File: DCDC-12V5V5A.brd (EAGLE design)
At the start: 40 x 23 mm, 37 parts, among them CN2 2828XX-2282834-2, CN3 2828XX-2282834-2, Q10 NMOSFET, Q9 NMOSFET, U1 LM3150MHX/NOPB

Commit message: Renamed 12V line to Vin. Generated CAM files.
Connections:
- net 12V renamed VIN
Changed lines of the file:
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@@
 </elements>
 <signals>
-<signal name="12V" airwireshidden="yes">
+<signal name="VIN" airwireshidden="yes">
 <contactref element="Q9" pad="4"/>
 <contactref element="U1" pad="2"/>

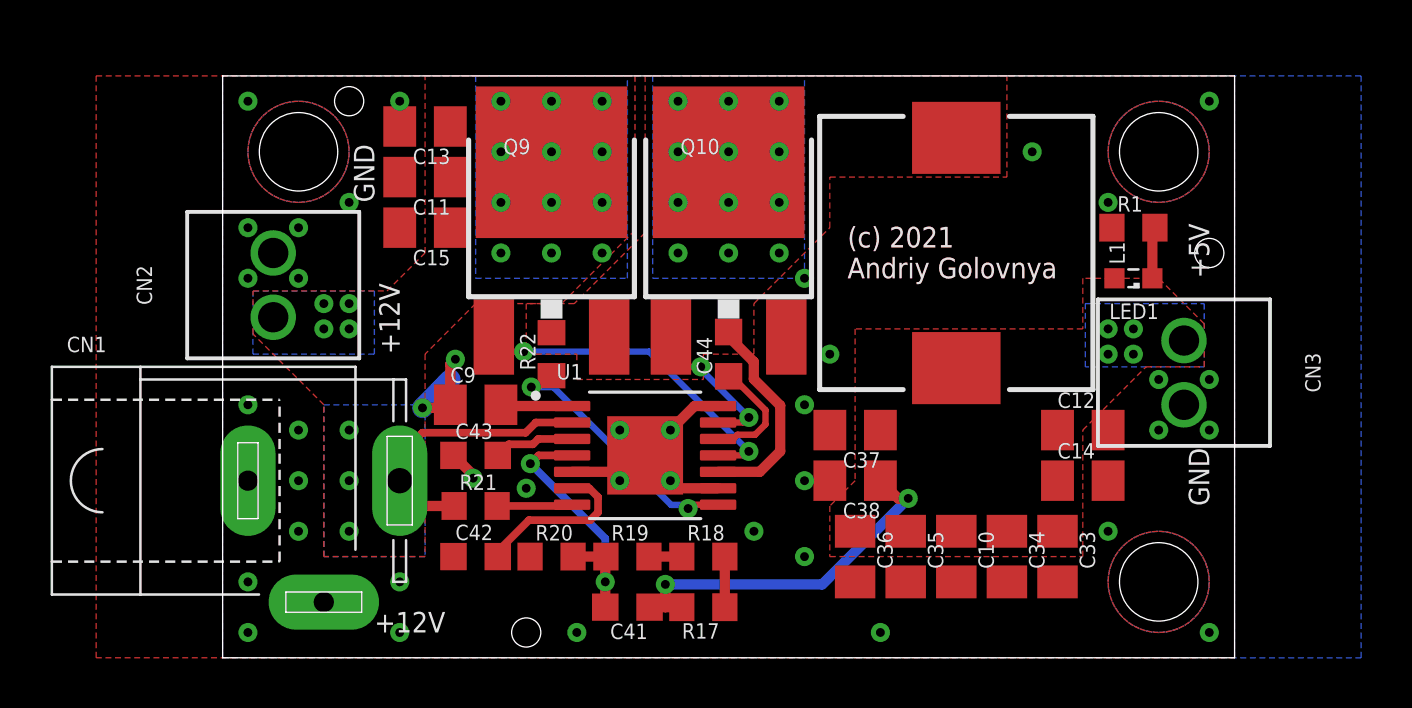
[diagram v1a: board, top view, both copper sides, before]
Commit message: Made new layout of DC-DC board. Improved XLS calculator. Generated CAM files. Generated BoM and PnP files. Generated PNG preview. Generated PDF schematics.
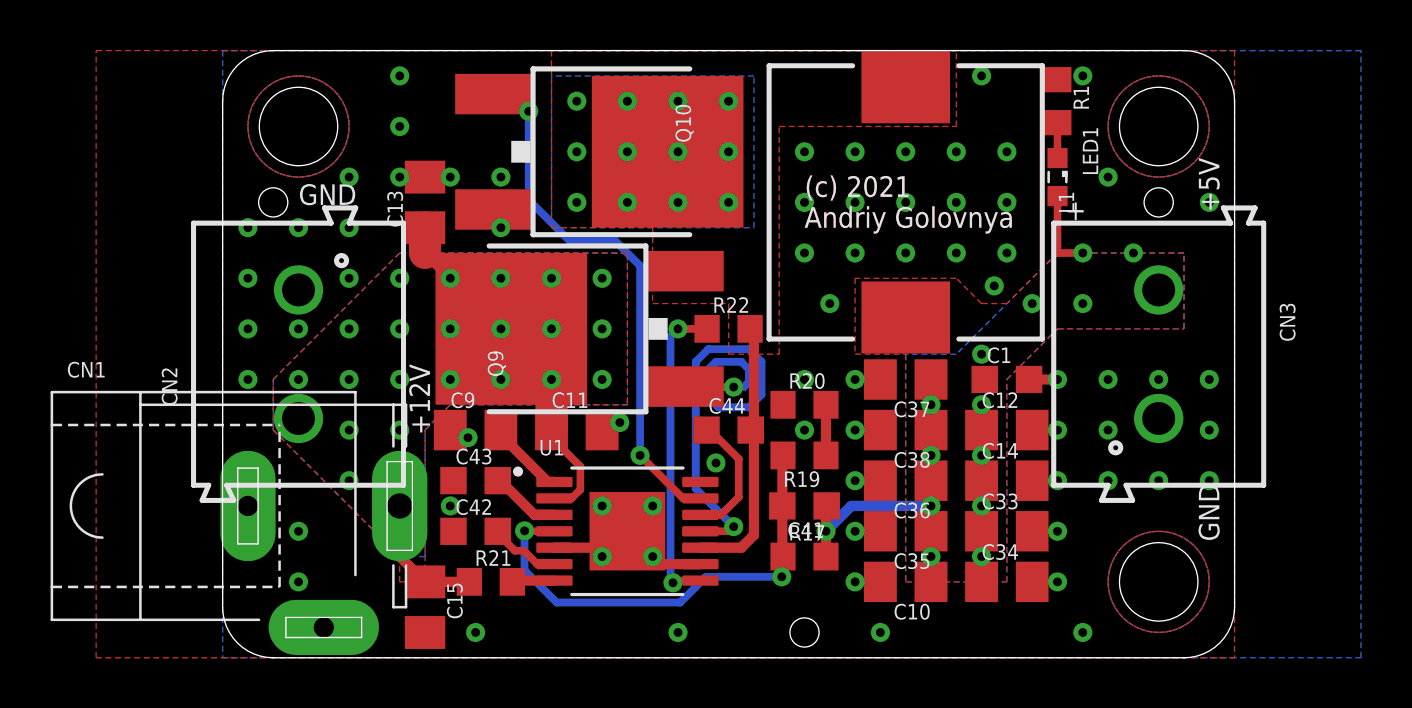
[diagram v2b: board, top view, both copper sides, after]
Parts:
- removed R18: 3k, rcl:R0603
- added C1: 1nF, rcl:C0603K
- CN2, CN3: value 2828XX-2282834-2 -> (none); device Connector:TERMBLK_254-2N -> Wurth_Connectors_WR-TBL Rising Cage Clamp:691213510002
- R1: value 3k -> 2k
- R17: value 68k -> 75k
- R19: value 3k -> 100
- moved C15 15.0 mm to (8.00, 2.00), turned to 270 degrees
- moved C11 11.7 mm to (14.0, 9.00), turned to 0 degrees
- moved R20 11.7 mm to (23.0, 10.0)
- moved HOLE3 11.0 mm to (23.0, 1.00)
- moved C41 8.06 mm to (23.0, 6.00)
- moved R19 8.06 mm to (23.0, 8.00), turned to 180 degrees
- moved R22 7.07 mm to (20.0, 13.0), turned to 0 degrees
- moved R1 5.83 mm to (33.0, 22.0), turned to 270 degrees
- moved HOLE2 5.00 mm to (2.00, 18.0)
- moved LED1 5.00 mm to (33.0, 19.0), turned to 270 degrees
- moved Q9 5.00 mm to (13.0, 13.0), turned to 90 degrees
- moved Q10 4.47 mm to (16.0, 20.0), turned to 270 degrees
- moved R17 4.47 mm to (23.0, 4.00), turned to 0 degrees
- moved CN2 4.12 mm to (3.00, 12.0)
- moved C36 3.61 mm to (27.0, 7.00), turned to 180 degrees
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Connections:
- net N$16 renamed BUCK_SS
- net N$18 renamed BUCK_EN
- net N$19 renamed BUCK_VCC
- net N$21 renamed BUCK_RON
- net N$23 renamed BUCK_BST
- net N$8 renamed BUCK_ILIM
- removed net N$13: R18.1, R19.2
- removed net N$9: R17.1, R18.2
- new net N$2: R19.1, R20.2
- net 5V: now also C1.1
- net BUCK_FB: now also R17.1, R19.2; no longer R19.1, R20.2
- net GND: now also C1.2
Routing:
- net BUCK_LG: track 6.23 -> 21.3 mm
- net BUCK_HG: track 13.3 -> 21.3 mm
- net BUCK_FB: track 11.0 -> 18.7 mm
- net GND: track 12.1 -> 5.16 mm, vias 40 -> 70
- net 5V: track 14.6 -> 9.82 mm, vias 6 -> 14
- net BUCK_SS: track 6.58 -> 2.83 mm
- net VIN: track 10.9 -> 13.6 mm, vias 19 -> 21
- net BUCK_SW: track 8.35 -> 10.6 mm
- net BUCK_ILIM: track 10.4 -> 12.5 mm
- net N$9: track 2.00 -> 0.00 mm
- net N$2: track 0.00 -> 2.00 mm
- net N$13: track 1.30 -> 0.00 mm
- net BUCK_RON: track 2.99 -> 1.72 mm
- net N$1: track 2.04 -> 1.40 mm
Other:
- board size 40 x 23 mm -> 40 x 24 mm
- board text added: "+"
- board text added: "DCDC-12V5V5A-0011"
- board text removed: "DCDC-12V5V5A-0010"

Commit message: Improved layout of DC-DC board. Rotated input terminal. Improved XLS calculator. Generated CAM files. Generated BoM and PnP files. Generated PNG preview. Generated PDF schematics.
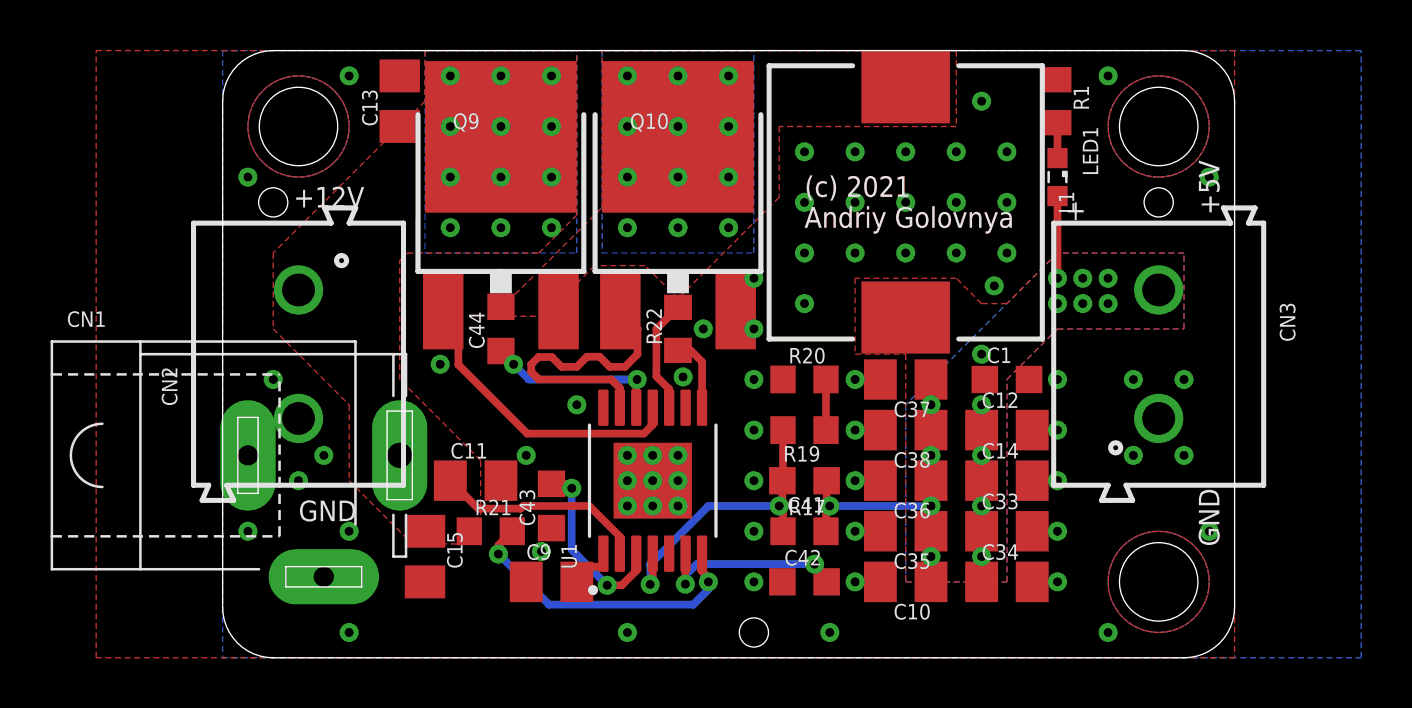
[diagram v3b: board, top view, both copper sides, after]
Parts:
- moved C42 13.2 mm to (23.0, 3.00)
- moved C44 9.85 mm to (11.0, 13.0), turned to 90 degrees
- moved C9 6.71 mm to (13.0, 3.00)
- moved Q9 6.32 mm to (11.0, 19.0), turned to 0 degrees
- moved C11 4.47 mm to (10.0, 7.00)
- moved C13 4.12 mm to (7.00, 22.0)
- moved C43 3.16 mm to (13.0, 6.00), turned to 90 degrees
- moved Q10 2.24 mm to (18.0, 19.0), turned to 0 degrees
- moved U1 2.24 mm to (17.0, 7.00), turned to 90 degrees
- moved C15 2.00 mm to (8.00, 4.00)
- moved CN1 2.00 mm to (4.00, 8.00)
- moved HOLE3 2.00 mm to (21.0, 1.00)
- moved R21 2.00 mm to (10.6, 5.00)
- moved R22 2.00 mm to (18.0, 13.0), turned to 90 degrees
- moved C41 1.00 mm to (23.0, 7.00)
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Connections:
- net GND: now also CN2.2; no longer CN2.1
- net VIN: now also CN2.1; no longer CN2.2
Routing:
- net BUCK_RON: track 1.72 -> 12.0 mm, vias 0 -> 2
- net BUCK_ILIM: track 12.5 -> 2.95 mm, vias 2 -> 0
- net BUCK_LG: track 21.3 -> 11.8 mm, vias 2 -> 0
- net BUCK_HG: track 21.3 -> 12.0 mm, vias 2 -> 0
- net BUCK_FB: track 18.7 -> 12.2 mm
- net BUCK_SW: track 10.6 -> 4.53 mm
- net VIN: track 13.6 -> 8.38 mm, vias 21 -> 12
- net GND: track 5.16 -> 0.00 mm, vias 70 -> 69
- net BUCK_SS: track 2.83 -> 7.75 mm, vias 0 -> 2
- net BUCK_EN: track 2.80 -> 7.35 mm, vias 0 -> 2
- net BUCK_BST: track 5.06 -> 6.99 mm, vias 0 -> 2
- net BUCK_VCC: track 3.08 -> 1.73 mm
- net 5V: track 9.82 -> 9.36 mm, vias 14 -> 16

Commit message: Moved some texts and tooling holes a bit. Generated CAM files. Generated PNG preview. Generated PDF schematics. Renamed BoM and PnP files.
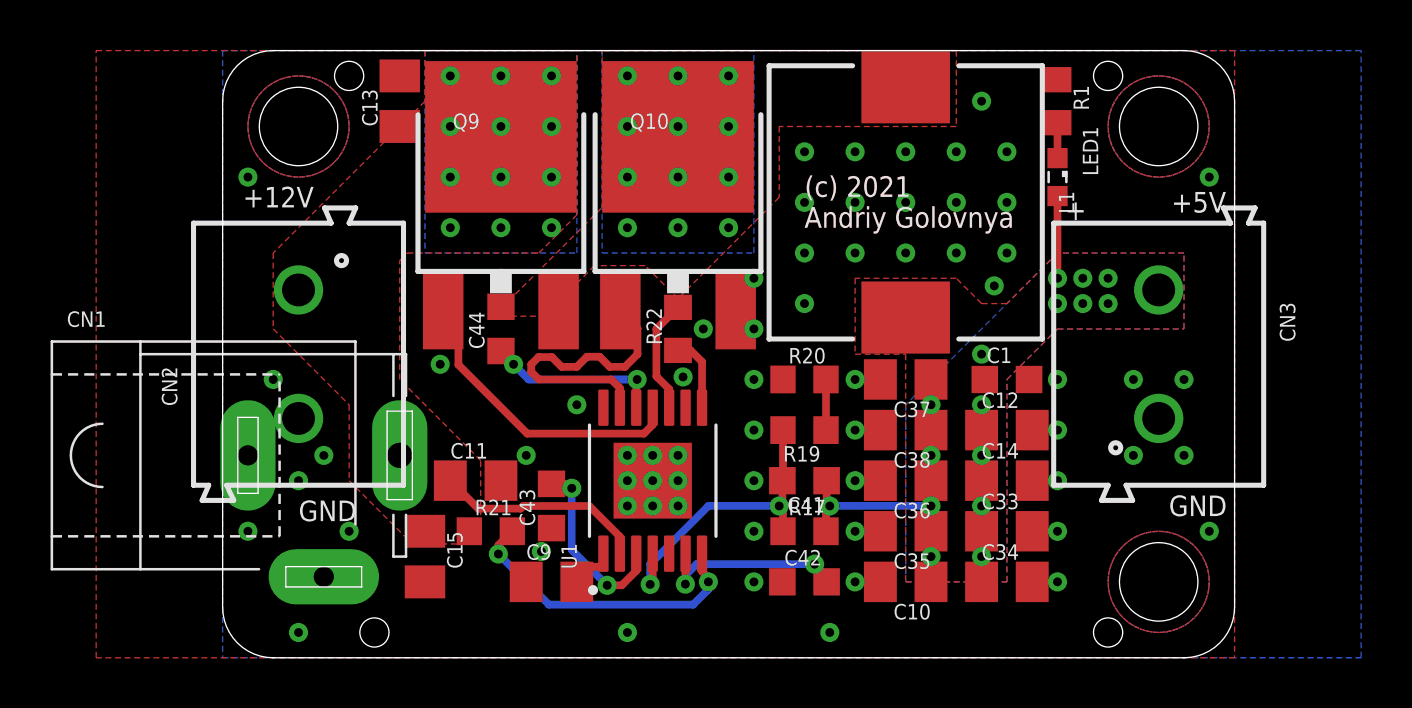
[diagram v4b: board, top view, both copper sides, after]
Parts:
- added HOLE4: TOOLINGHOLE, _my_fiducia:TOOLING-HOLE
- moved HOLE3 15.0 mm to (6.00, 1.00)
- moved HOLE2 5.83 mm to (5.00, 23.0)
- moved HOLE1 5.39 mm to (35.0, 23.0)
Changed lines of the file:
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@@
 <drawing>
 <settings>
-<setting alwaysvectorfont="yes"/>
+<setting alwaysvectorfont="no"/>
 <setting verticaltext="up"/>
 </settings>
@@
 <hole x="37" y="3" drill="3.1"/>
 <text x="33" y="20" size="1.6764" layer="22" font="vector" ratio="20" rot="MR0">DCDC-12V5V5A-0011</text>
-<text x="2.8" y="17.8" size="0.8128" layer="21" font="vector">+12V</text>
+<text x="0.8" y="17.8" size="0.8128" layer="21" font="vector">+12V</text>
 <text x="3" y="5.4" size="0.8128" layer="21" font="vector">GND</text>
-<text x="39.4" y="4.4" size="0.8128" layer="21" font="vector" rot="R90">GND</text>
-<text x="39.4" y="17.5" size="0.8128" layer="21" font="vector" rot="R90">+5V</text>
+<text x="37.4" y="5.6" size="0.8128" layer="21" font="vector">GND</text>
+<text x="37.5" y="17.6" size="0.8128" layer="21" font="vector">+5V</text>
 <text x="33" y="16" size="1.27" layer="22" font="vector" rot="MR0">(c) Andriy Golovnya</text>
 <text x="33" y="18" size="1.27" layer="22" font="vector" rot="MR0">5V/5A DC-DC Buck Converter</text>
@@
 <attribute name="VALUE" x="31.095" y="22.635" size="0.6096" layer="27" font="vector" rot="R270"/>
 </element>
-<element name="HOLE1" library="_my_fiducia" package="TOOLING-HOLE" value="TOOLINGHOLE" x="37" y="18" smashed="yes"/>
-<element name="HOLE2" library="_my_fiducia" package="TOOLING-HOLE" value="TOOLINGHOLE" x="2" y="18" smashed="yes"/>
-<element name="HOLE3" library="_my_fiducia" package="TOOLING-HOLE" value="TOOLINGHOLE" x="21" y="1" smashed="yes"/>
+<element name="HOLE1" library="_my_fiducia" package="TOOLING-HOLE" value="TOOLINGHOLE" x="35" y="23" smashed="yes"/>
+<element name="HOLE2" library="_my_fiducia" package="TOOLING-HOLE" value="TOOLINGHOLE" x="5" y="23" smashed="yes"/>
+<element name="HOLE3" library="_my_fiducia" package="TOOLING-HOLE" value="TOOLINGHOLE" x="6" y="1" smashed="yes"/>
 <element name="C1" library="rcl" library_urn="urn:adsk.eagle:library:334" package="C0603K" package3d_urn="urn:adsk.eagle:package:23680/2" value="1nF" x="31" y="11" smashed="yes">
 <attribute name="NAME" x="30.2" y="11.65" size="0.6096" layer="25" font="vector"/>
@@
 <attribute name="VALUE" x="30.2" y="9.35" size="0.6096" layer="27" font="vector"/>
 </element>
+<element name="HOLE4" library="_my_fiducia" package="TOOLING-HOLE" value="TOOLINGHOLE" x="35" y="1" smashed="yes"/>
 </elements>
 <signals>
@@
 <via x="33" y="5" extent="1-16" drill="0.35"/>
 <via x="33" y="3" extent="1-16" drill="0.35"/>
-<via x="5" y="23" extent="1-16" drill="0.35"/>
 <via x="30.5" y="14.7" extent="1-16" drill="0.35"/>
 <via x="30" y="22" extent="1-16" drill="0.35"/>
-<via x="35" y="23" extent="1-16" drill="0.35"/>
 <via x="39" y="19" extent="1-16" drill="0.35"/>
 <via x="39" y="5" extent="1-16" drill="0.35"/>
@@
 <via x="1" y="5" extent="1-16" drill="0.35"/>
 <via x="1" y="19" extent="1-16" drill="0.35"/>
-<via x="35" y="1" extent="1-16" drill="0.35"/>
 <via x="17" y="8" extent="1-16" drill="0.35"/>
 <via x="17" y="7" extent="1-16" drill="0.35"/>
@@
 <via x="4" y="8" extent="1-16" drill="0.35"/>
 <via x="2" y="11" extent="1-16" drill="0.35"/>
-<via x="5" y="1" extent="1-16" drill="0.35"/>
+<via x="3" y="1" extent="1-16" drill="0.35"/>
 <via x="12" y="8" extent="1-16" drill="0.35"/>
 <via x="12.6" y="4.2" extent="1-16" drill="0.35"/>

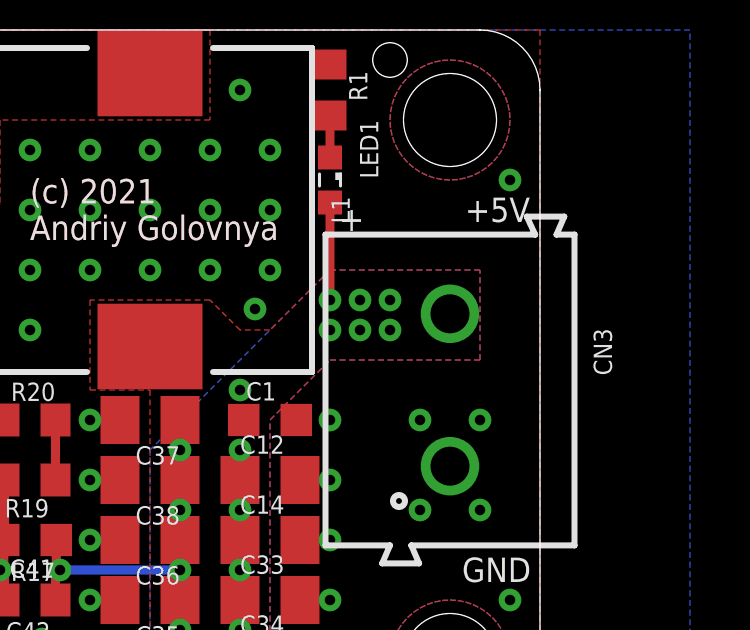
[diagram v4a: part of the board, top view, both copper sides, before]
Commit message: Added few vias. Generated CAM files. Generated PNG preview. Renamed BoM and PnP files.
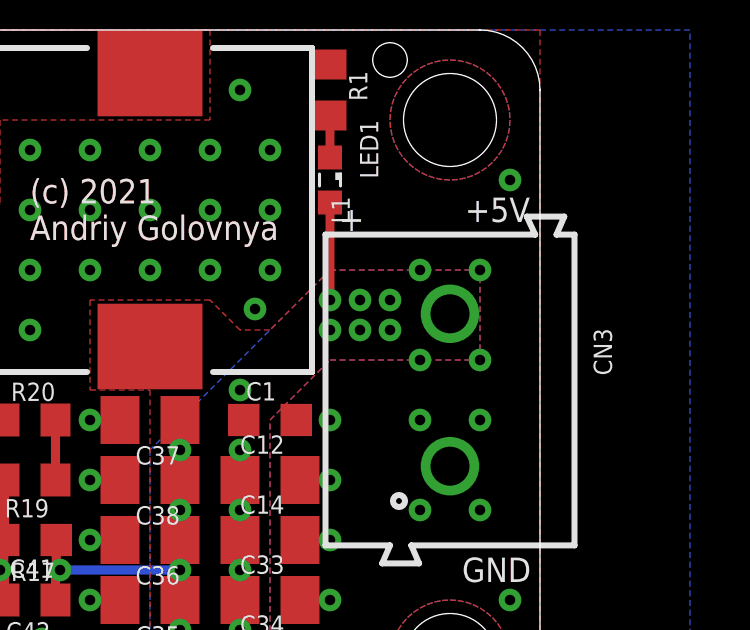
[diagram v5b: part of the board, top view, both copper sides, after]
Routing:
- net 5V: vias 16 -> 20
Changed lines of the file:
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@@
 <drawing>
 <settings>
-<setting alwaysvectorfont="no"/>
+<setting alwaysvectorfont="yes"/>
 <setting verticaltext="up"/>
 </settings>
@@
 <via x="30" y="12" extent="1-16" drill="0.35"/>
 <wire x1="33" y1="18.25" x2="33" y2="15" width="0.3048" layer="1"/>
+<via x="38" y="16" extent="1-16" drill="0.35"/>
+<via x="36" y="16" extent="1-16" drill="0.35"/>
+<via x="36" y="13" extent="1-16" drill="0.35"/>
+<via x="38" y="13" extent="1-16" drill="0.35"/>
 </signal>
 <signal name="BUCK_LG">
